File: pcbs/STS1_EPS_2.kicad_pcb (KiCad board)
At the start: 6 copper layers, 81 x 85 mm, 151 parts, among them J1 DS1, J2 DS2, J5 RBF, J6 Antenna Deployment, J7 Inter-EPS, J9 Battery Pack, Q1 2N7002, Q10 2N7002, Q11 2N7002, Q14 2N7002, Q15 2N7002, Q18 2N7002, Q19 2N7002, Q2 SI7272DP-T1-GE3, Q20 2N7002, Q21 SI7272DP-T1-GE3, Q22 SI7272DP-T1-GE3, Q3 2N7002, Q5 SI7135DP-T1-GE3, Q6 2N7002, Q7 2N7002, U1 4072, U11 LTC4451AV#TRMPBF, U12 LTC4451AV#TRMPBF, U13 4082, U2 LTC6995IDCB-1, U3 TPS2420RSAT, U4 MIC841H, U5 MIC841H, U6 TPS2420RSAT, U7 BQ29209DRBT, U8 4072

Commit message: Logic gates now use ISO symbols consistently.
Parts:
- C10, C12, C13, C15, C16, C18, C19, C21, C22, C8, C9: value C -> 680n
- C11, C14, C17, C20, C7: value C_Polarized -> 680u
- D2: value ~ -> VESD05A8A-HNH-GS08
- F1: value Fuse -> CC12H250mA-TR
- R13, R40: value 64k -> 63k4
- R14, R39: value 31k5 -> 31k6

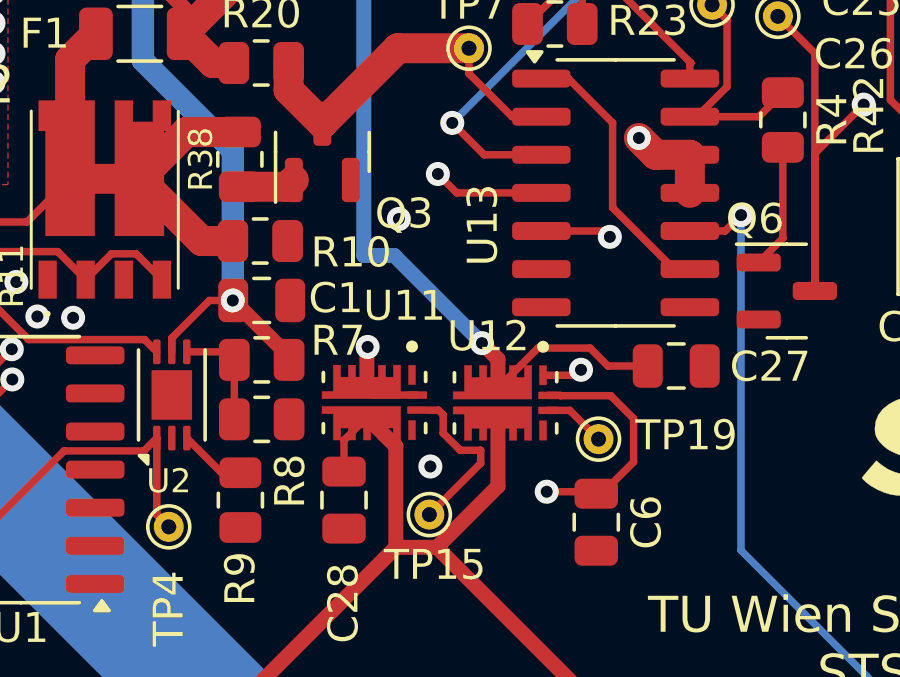
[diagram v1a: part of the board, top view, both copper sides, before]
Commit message: Separated the SHDN pins of the logic- and power oring. Also added TVS diodes to them, as this is recommended by the datasheet.
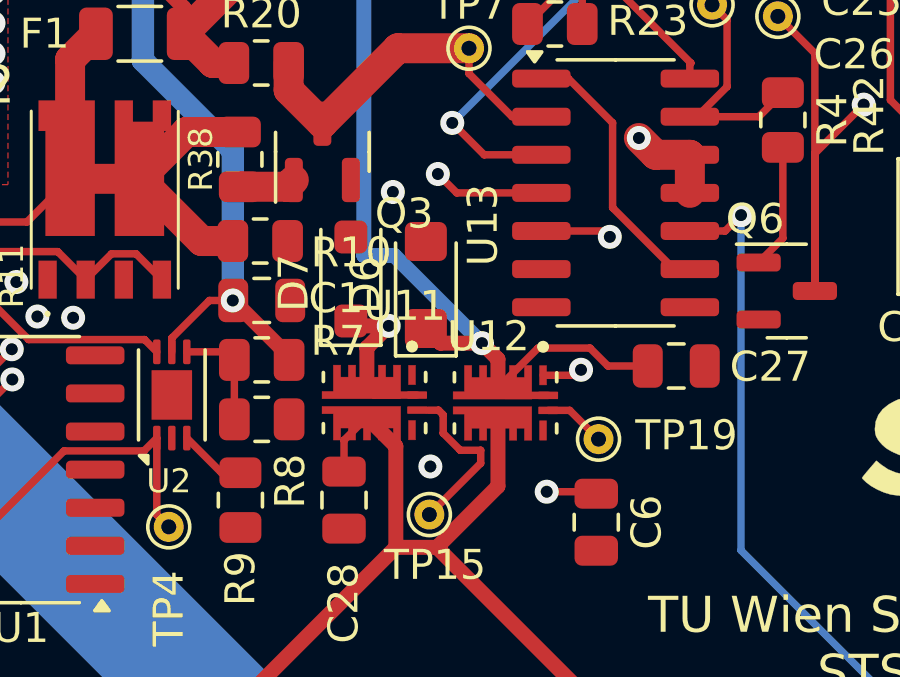
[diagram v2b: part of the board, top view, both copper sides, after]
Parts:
- added D6: SMF5.0A, Diode_SMD:D_SMF, F.Cu at (158.7, 81.6)
- added D7: SMF8.0A-HF, Diode_SMD:D_SOD-123F, F.Cu at (156.2, 81.4)
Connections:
- U12 pad 16: /BATT_RAW -> /MPPT_BUS
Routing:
- net /BATT_RAW: track 279.0 -> 274.4 mm
- net /MPPT_BUS: track 73.1 -> 76.9 mm

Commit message: Added a linear regulator to the power oring in STS1_EPS_2, since the components supplied by that power oring could not withstand that voltage.
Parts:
- added C29: 1u, Capacitor_SMD:C_0805_2012Metric, F.Cu at (154.9, 92.9)
- added C30: 1u, Capacitor_SMD:C_0805_2012Metric, F.Cu at (166.8, 94.2)
- added TP29: TestPoint, TestPoint:TestPoint_THTPad_D1.0mm_Drill0.5mm, F.Cu at (155.2, 95.3)
- added TP30: TestPoint, TestPoint:TestPoint_THTPad_D1.0mm_Drill0.5mm, F.Cu at (169.4, 92.4)
- added U9: BD50GA5WEFJ, Package_SO:HTSOP-8-1EP_3.9x4.9mm_P1.27mm_EP2.4x3.2mm, F.Cu at (161.2, 92.9)
- moved C6 2.32 mm to (166.7, 89.6)
- moved TP15 0.32 mm to (159.1, 89.1)
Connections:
- C28 pad 1: /V_LOGIC -> Net-(U11-OUT)
- U11 pad 8: /V_LOGIC -> Net-(U11-OUT)
- U12 pad 8: /V_LOGIC -> Net-(U11-OUT)
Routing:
- net Net-(U11-OUT): track 0.00 -> 24.0 mm
- net /V_LOGIC: track 382.7 -> 376.7 mm
- net /BATT_RAW: track 274.4 -> 276.8 mm
- net Net-(U11-STATUS): track 5.53 -> 4.45 mm

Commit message: Added more part numbers.
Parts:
- R3: footprint Capacitor_SMD:C_0805_2012Metric -> Resistor_SMD:R_0805_2012Metric
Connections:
- J2 pad 1: /Deployment Switches + RBF/DS2+ -> GND
- J2 pad 2: GND -> /Deployment Switches + RBF/DS2+
- J5 pad 1: /Deployment Switches + RBF/RBF+ -> GND
- J5 pad 2: GND -> /Deployment Switches + RBF/RBF+
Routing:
- net GND: vias 29 -> 30

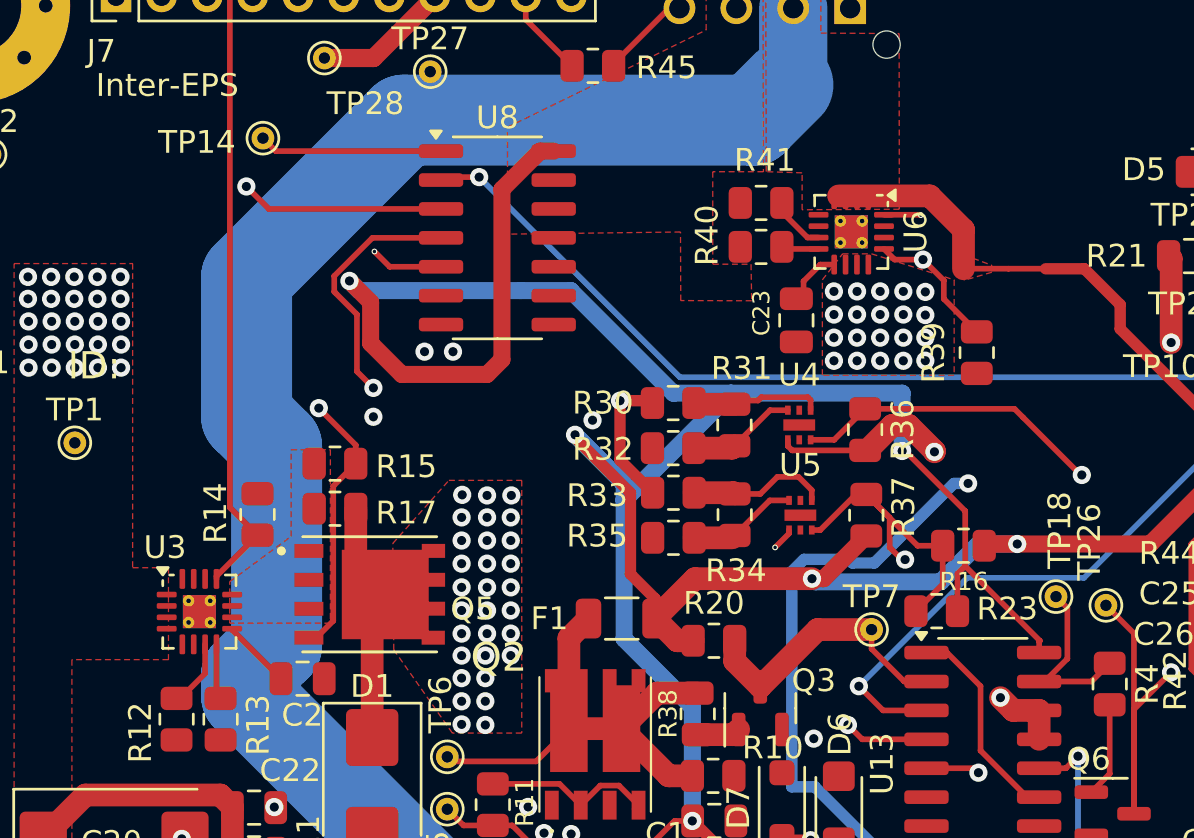
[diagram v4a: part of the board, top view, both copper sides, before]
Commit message: Fixed footprint of U3 and U6 on STS1_EPS_2.
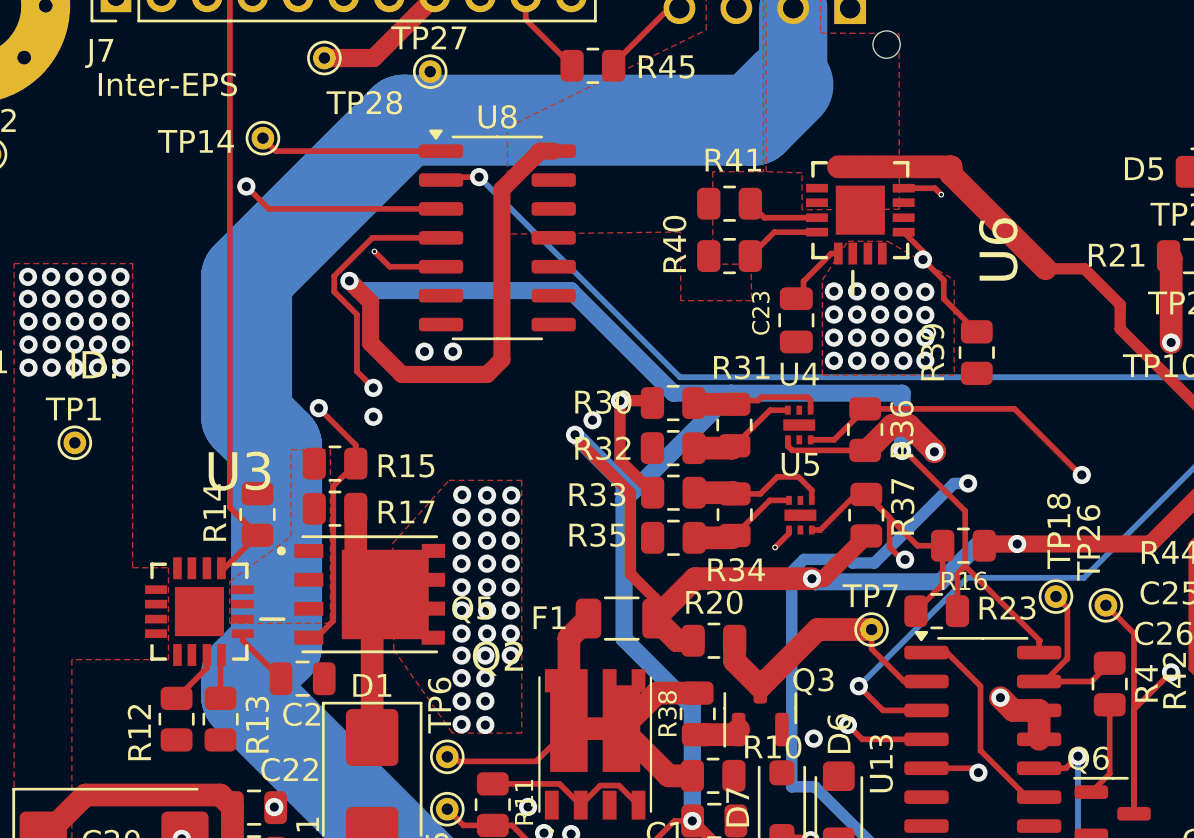
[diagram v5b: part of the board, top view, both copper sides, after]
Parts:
- U3, U6: footprint Package_DFN_QFN:VQFN-16-1EP_3x3mm_P0.5mm_EP1.45x1.45mm_ThermalVias -> STS_Package_DFN_QFN:QFN65P400X400X100-17N
- moved R40 1.44 mm to (153.9, 57.3)
- moved R41 1.38 mm to (153.9, 55.0)
- moved U6 1.03 mm to (159.6, 55.3)
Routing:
- net /Battery/IFLT: track 1.65 -> 3.36 mm
- net /Battery/IMAX: track 2.47 -> 3.18 mm
- net /Battery/~{BATT_INHIBIT}: track 40.0 -> 40.7 mm
- net /Bus Gate/IMAX: track 2.99 -> 2.46 mm
